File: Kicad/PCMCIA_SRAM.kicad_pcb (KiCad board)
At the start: 2 copper layers, 41.9 x 44.5 mm, 21 parts, among them J1 PCMCIA, J2 JTAG, U1 SPX3819M5-L-3-3, U2 XC9536XL-VQ44, U3 CY62177ESL-55ZXI, U4 CY62167ELL-45ZXI

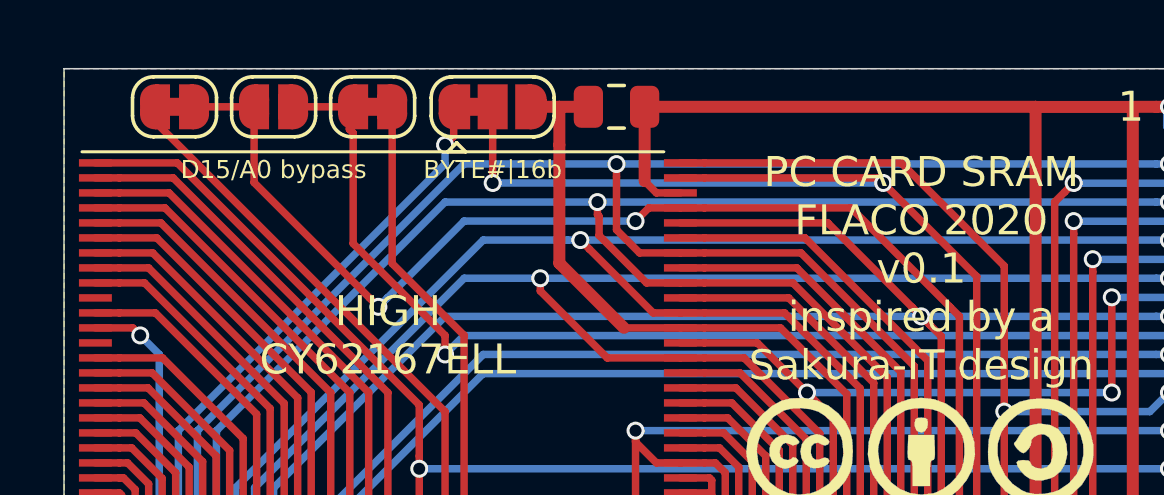
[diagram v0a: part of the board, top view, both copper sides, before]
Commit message: v1.0 KiCAD files, D15/A0 bypass by default
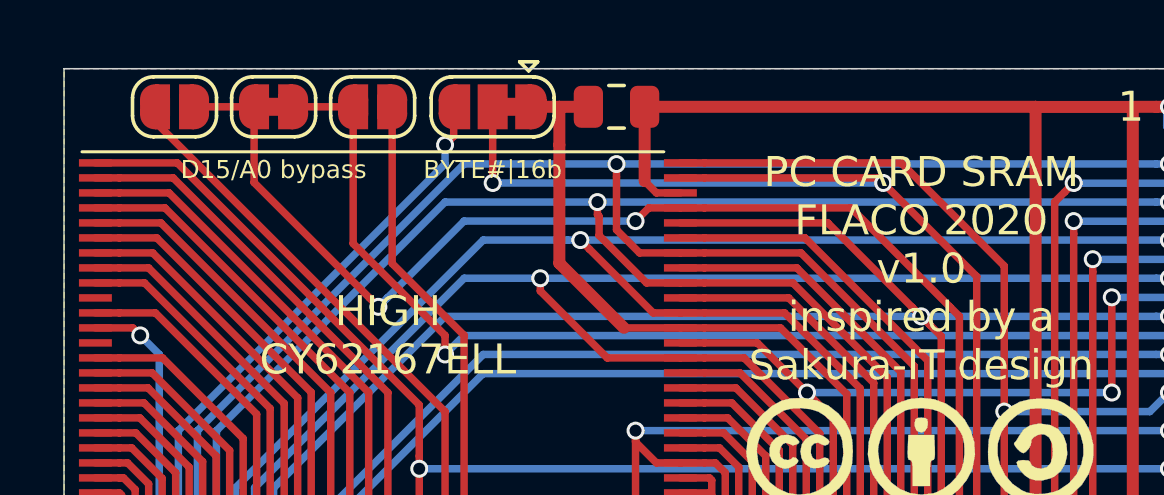
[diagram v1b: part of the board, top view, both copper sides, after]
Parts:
- JP1, JP3: footprint Jumper:SolderJumper-2_P1.3mm_Bridged_RoundedPad1.0x1.5mm -> Jumper:SolderJumper-2_P1.3mm_Open_RoundedPad1.0x1.5mm
- JP2: footprint Jumper:SolderJumper-2_P1.3mm_Open_RoundedPad1.0x1.5mm -> Jumper:SolderJumper-2_P1.3mm_Bridged_RoundedPad1.0x1.5mm
- turned JP7 to 180 degrees
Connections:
- JP7 pad 1: /_BYTE_A -> +5V
- JP7 pad 3: +5V -> /_BYTE_A
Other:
- board text added: "PC CARD SRAM FLACO 2020 v1.0 inspired by a Sakura-IT design"
- board text removed: "PC CARD SRAM FLACO 2020 v0.1 inspired by a Sakura-IT design"

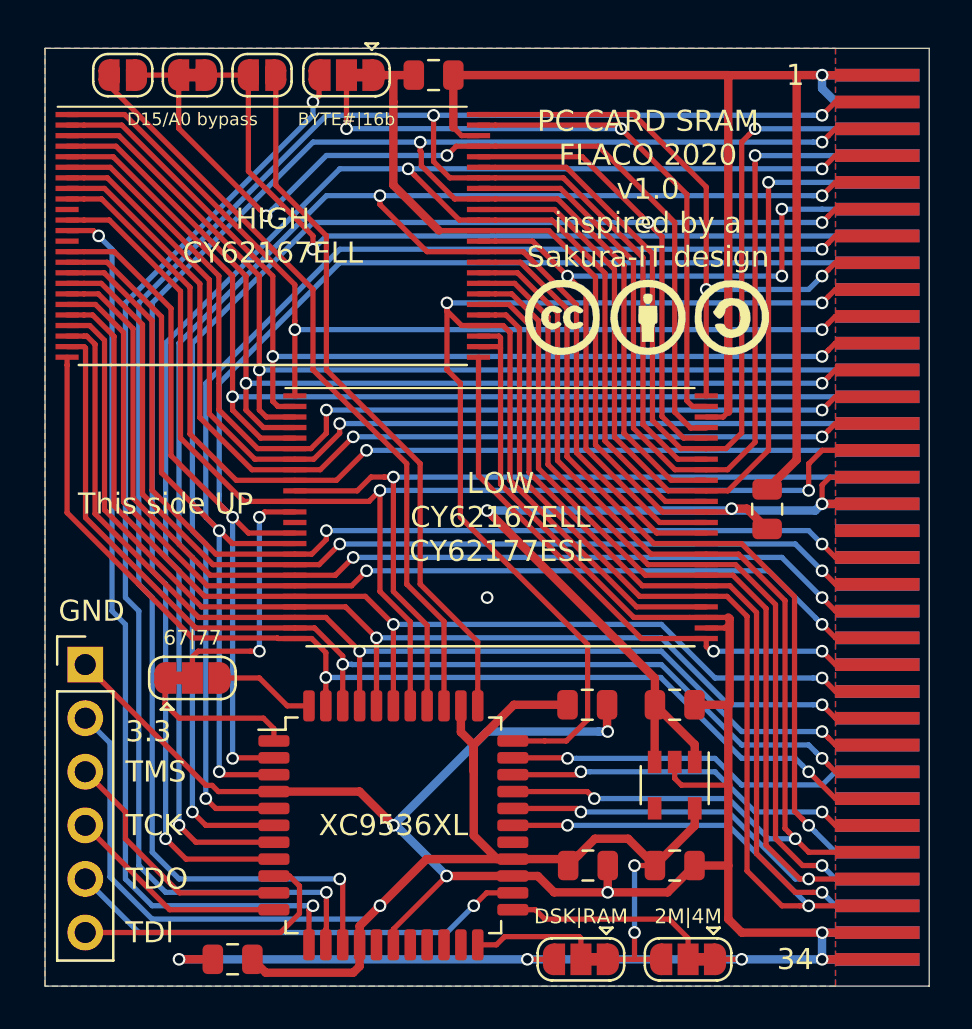
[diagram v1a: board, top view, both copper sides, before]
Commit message: Made pads shorter on PCMCIA connector. Corrected license to CC-BY-NC-SA.
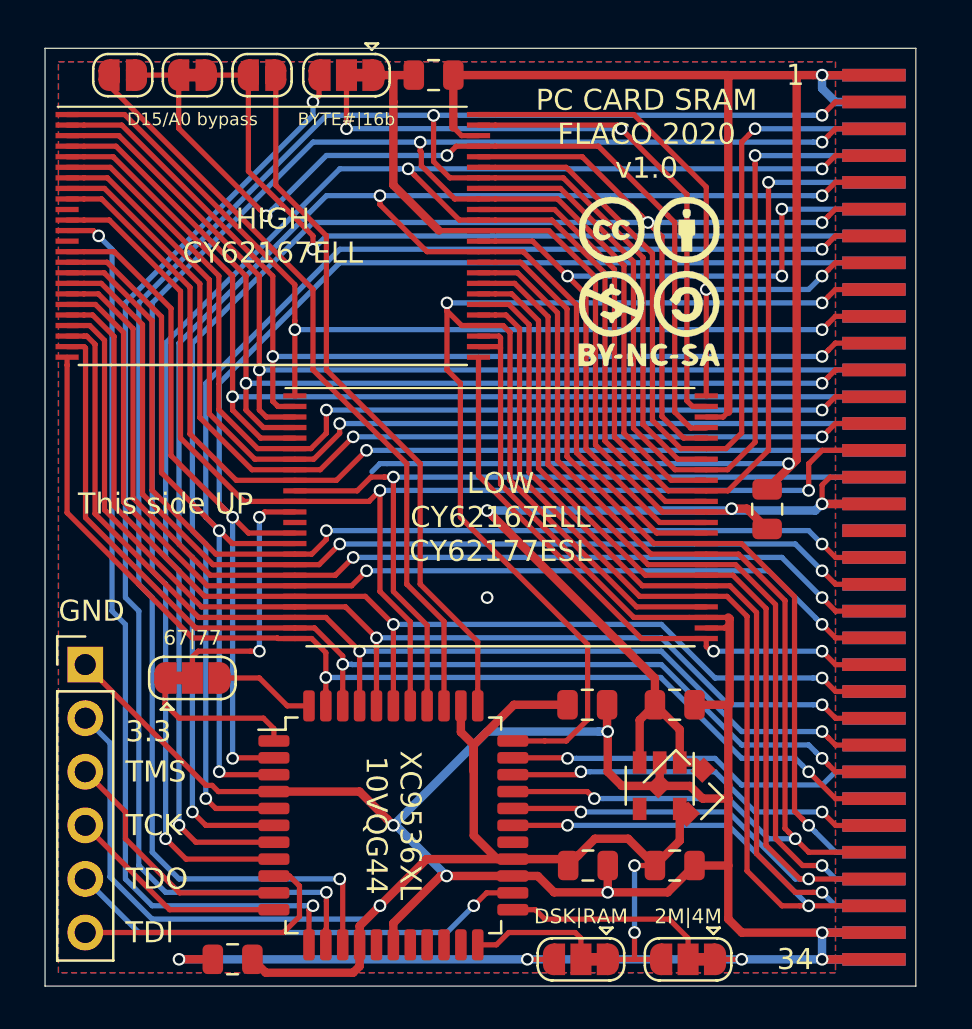
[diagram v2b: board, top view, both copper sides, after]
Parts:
- added FID2: Logo, Sassa:PIC_Cassepanards_GS, B.Cu at (185.4, 103.5)
- added U11: XC6206PxxxMR, Package_TO_SOT_SMD:SOT-23, F.Cu at (196.2, 116.2)
- FID1: footprint Sassa:CC_BY_SA_long_silkscreen_14x5.5mm -> Sassa:CC_BY_NC_SA_square_silkscreen
- J1: footprint Sassa:pcmcia -> Sassa:PCMCIA_female_edge_connector; moved to B.Cu
- moved J1 5.08 mm to (207.6, 103.5)
- moved FID1 1.65 mm to (194.4, 92.3)
- moved U1 0.71 mm to (194.9, 116.2)
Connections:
- J1 pad 18: (no net) -> Net-(J1-Pad18)
- J1 pad 43: (no net) -> /_VS1
- J1 pad 44: (no net) -> Net-(J1-Pad44)
- J1 pad 45: (no net) -> Net-(J1-Pad45)
- J1 pad 52: (no net) -> Net-(J1-Pad52)
- J1 pad 53: (no net) -> /A22
- J1 pad 54: (no net) -> /A23
- J1 pad 55: (no net) -> /A24
- J1 pad 56: (no net) -> /A25
- J1 pad 57: (no net) -> /_VS2
- J1 pad 58: (no net) -> /RESET
- J1 pad 59: (no net) -> /_WAIT
- J1 pad 60: (no net) -> Net-(J1-Pad60)
- J1 pad 62: (no net) -> /BVD2
- J1 pad 63: (no net) -> /BVD1
- U1 pad 4: (no net) -> Net-(U1-Pad4)
- U2 pad 16: (no net) -> Net-(U2-Pad16)
- U2 pad 18: (no net) -> Net-(U2-Pad18)
- U2 pad 19: (no net) -> Net-(U2-Pad19)
- U2 pad 20: (no net) -> Net-(U2-Pad20)
- U2 pad 21: (no net) -> Net-(U2-Pad21)
- U2 pad 27: (no net) -> Net-(U2-Pad27)
- U3 pad 13: (no net) -> Net-(U3-Pad13)
- U4 pad 10: (no net) -> Net-(U4-Pad10)
- U4 pad 13: (no net) -> Net-(U4-Pad13)
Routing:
- net GND: track 223.2 -> 243.4 mm, vias 11 -> 12
- net /_OE: track 71.0 -> 69.6 mm
- net /_CE1: track 78.0 -> 76.5 mm
- net /D7: track 83.0 -> 81.5 mm
- net /D6: track 90.6 -> 89.1 mm
- net /D5: track 92.0 -> 90.5 mm
- net /D4: track 95.7 -> 94.3 mm
- net /D2: track 58.6 -> 57.1 mm
- net /D1: track 57.7 -> 56.3 mm
- net /D0: track 56.3 -> 54.9 mm
- net /A9: track 50.0 -> 48.5 mm
- net /A8: track 51.5 -> 50.1 mm
- net /A7: track 51.5 -> 50.1 mm
- net /A6: track 29.7 -> 28.3 mm
- net /A5: track 55.6 -> 54.2 mm
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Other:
- board size 41.9 x 44.5 mm -> 41.3 x 44.5 mm
- board text added: "PC CARD SRAM FLACO 2020 v1.0"
- board text added: "XC9536XL 10VQG44"
- board text removed: "PC CARD SRAM FLACO 2020 v1.0 inspired by a Sakura-IT design"
- board text removed: "XC9536XL"

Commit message: Kicad: conversion to Kicad 6 ; repo URL on PCB silkscreen.
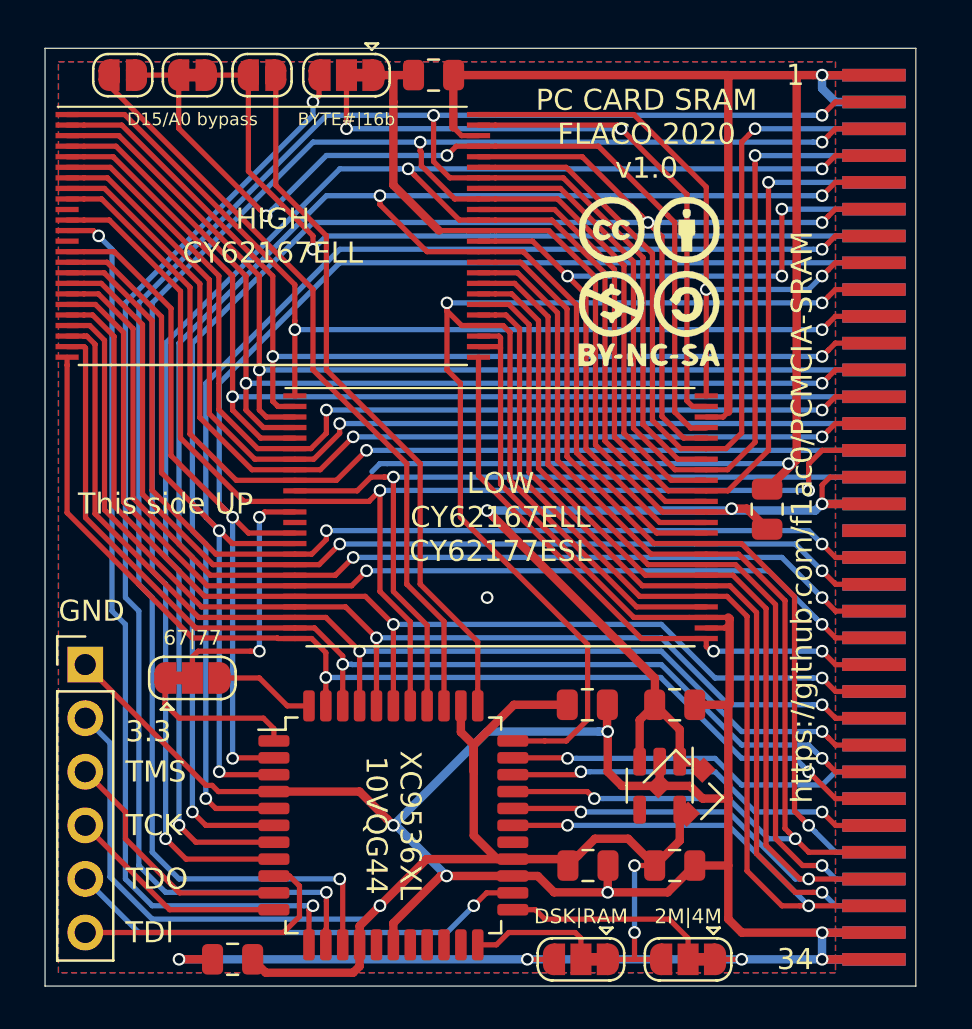
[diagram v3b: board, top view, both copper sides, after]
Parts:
- U11: footprint Package_TO_SOT_SMD:SOT-23 -> Sassa:SOT-23
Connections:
- net +3V3 renamed +3.3V
- J1 pad 18: Net-(J1-Pad18) -> unconnected-(J1-Pad18)
- J1 pad 44: Net-(J1-Pad44) -> unconnected-(J1-Pad44)
- J1 pad 45: Net-(J1-Pad45) -> unconnected-(J1-Pad45)
- J1 pad 52: Net-(J1-Pad52) -> unconnected-(J1-Pad52)
- J1 pad 60: Net-(J1-Pad60) -> unconnected-(J1-Pad60)
- U1 pad 4: Net-(U1-Pad4) -> unconnected-(U1-Pad4)
- U2 pad 16: Net-(U2-Pad16) -> unconnected-(U2-Pad16)
- U2 pad 18: Net-(U2-Pad18) -> unconnected-(U2-Pad18)
- U2 pad 19: Net-(U2-Pad19) -> unconnected-(U2-Pad19)
- U2 pad 20: Net-(U2-Pad20) -> unconnected-(U2-Pad20)
- U2 pad 21: Net-(U2-Pad21) -> unconnected-(U2-Pad21)
- U2 pad 27: Net-(U2-Pad27) -> unconnected-(U2-Pad27)
- U3 pad 13: Net-(U3-Pad13) -> unconnected-(U3-Pad13)
- U4 pad 10: Net-(U4-Pad10) -> unconnected-(U4-Pad10)
- U4 pad 13: Net-(U4-Pad13) -> unconnected-(U4-Pad13)
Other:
- net class Default removed
- board text added: "https://github.com/f1ac0/PCMCIA-SRAM"
